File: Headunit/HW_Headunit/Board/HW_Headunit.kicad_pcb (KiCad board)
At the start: 2 copper layers, 27 x 30 mm, 4 parts, among them J1 AudioJack4_SwitchT1, J2 AudioJack4_SwitchT1, J3 2328702-8, U2 PY32F002AW15U

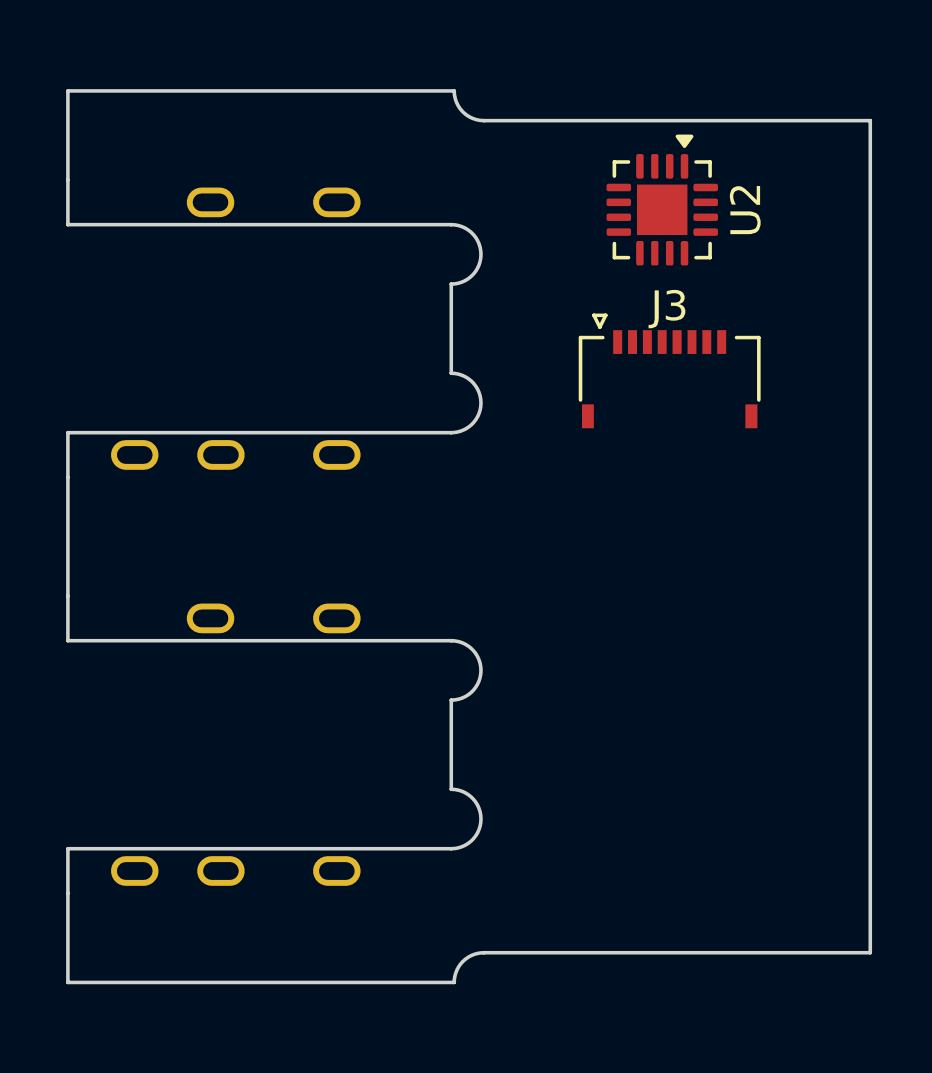
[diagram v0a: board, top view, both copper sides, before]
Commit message: PCB shape improved
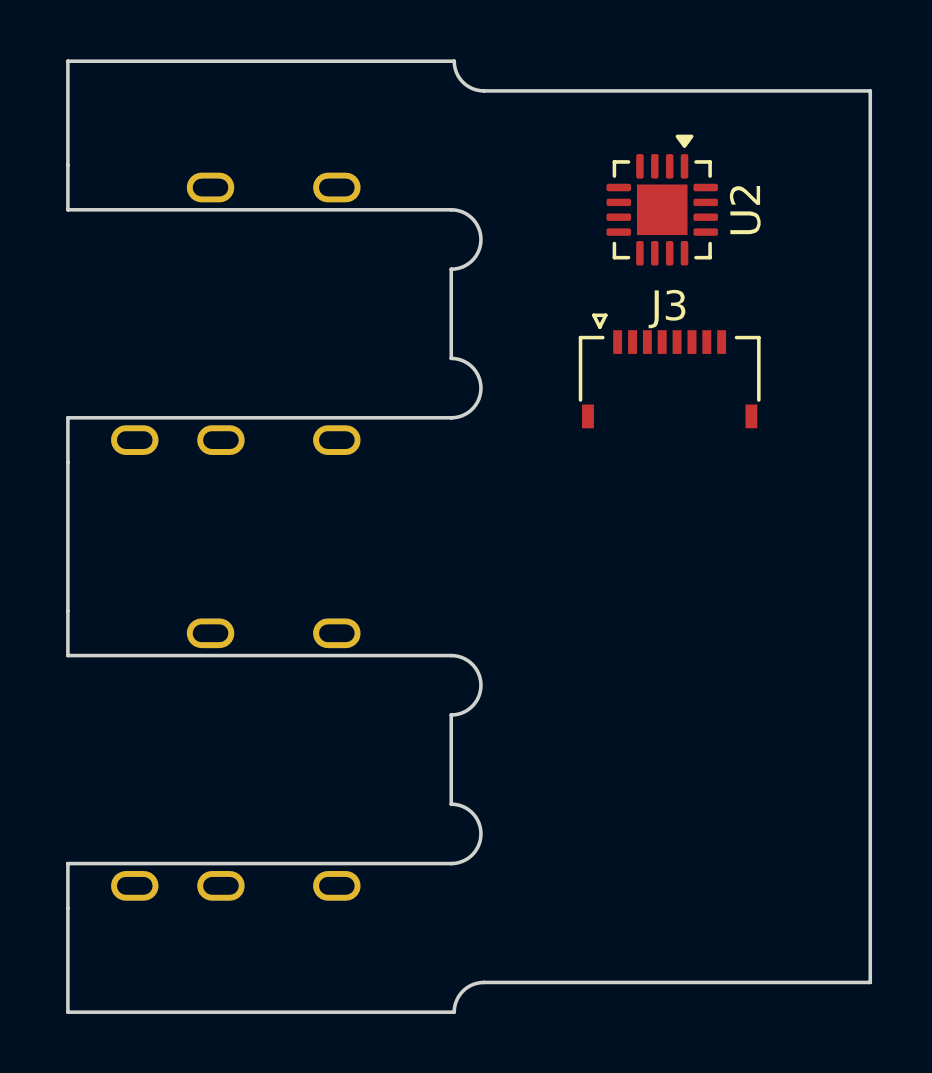
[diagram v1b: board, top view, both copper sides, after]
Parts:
- moved J1 0.50 mm to (0.00, 7.50)
- moved J2 0.50 mm to (0.00, -7.50)
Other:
- board size 27 x 30 mm -> 27 x 32 mm
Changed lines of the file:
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@@
 	(footprint "USER:XB-PJ-1837"
 		(layer "B.Cu")
-		(at 0 -7 -90)
+		(at 0 -7.5 -90)
 		(descr "TRS 3.5mm, horizontal, through-hole, https://www.cuidevices.com/product/resource/pdf/sj1-352xn.pdf")
 		(tags "TRS audio jack stereo horizontal")
@@
 	(footprint "USER:XB-PJ-1837"
 		(layer "B.Cu")
-		(at 0 7 -90)
+		(at 0 7.5 -90)
 		(descr "TRS 3.5mm, horizontal, through-hole, https://www.cuidevices.com/product/resource/pdf/sj1-352xn.pdf")
 		(tags "TRS audio jack stereo horizontal")
@@
 	)
 	(gr_line
-		(start 14 -14)
-		(end 27 -14)
+		(start 14.000001 -15)
+		(end 27.000001 -15)
 		(stroke
 			(width 0.12)
@@
 	)
 	(gr_line
-		(start 0 12)
-		(end 0 15)
+		(start 0 12.5)
+		(end 0 16)
 		(stroke
 			(width 0.12)
@@
 	)
 	(gr_arc
-		(start 13 15)
-		(mid 13.292893 14.292893)
-		(end 14 14)
+		(start 13 16)
+		(mid 13.292893 15.292893)
+		(end 14 15)
 		(stroke
 			(width 0.12)
@@
 	)
 	(gr_line
-		(start 0 -12)
-		(end 0 -15)
+		(start 0 -12.5)
+		(end 0 -16)
 		(stroke
 			(width 0.12)
@@
 	)
 	(gr_line
-		(start 27 14)
-		(end 27 -14)
+		(start 27 15)
+		(end 27.000001 -15)
 		(stroke
 			(width 0.12)
@@
 	)
 	(gr_line
-		(start 14 14)
-		(end 27 14)
+		(start 14 15)
+		(end 27 15)
 		(stroke
 			(width 0.12)
@@
 	)
 	(gr_line
-		(start 0 -15)
-		(end 13 -15)
+		(start 0 -16)
+		(end 13 -16)
 		(stroke
 			(width 0.12)
@@
 	)
 	(gr_arc
-		(start 13.999999 -14)
-		(mid 13.292893 -14.292894)
-		(end 12.999999 -15)
+		(start 14 -15)
+		(mid 13.292894 -15.292894)
+		(end 13 -16)
 		(stroke
 			(width 0.12)
@@
 	)
 	(gr_line
-		(start 0 15)
-		(end 13 15)
+		(start 0 16)
+		(end 13 16)
 		(stroke
 			(width 0.12)
@@
 	)
 	(gr_line
-		(start 0 2)
-		(end 0 -2)
-		(stroke
-			(width 0.12)
+		(start 0 2.5)
+		(end 0 -2.5)
+		(stroke
+			(width 0.12)

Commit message: Exported fabrication files
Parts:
- added C1: 1u, Capacitor_SMD:C_0603_1608Metric, F.Cu at (6.00, 14.2)
- added C2: 100n, Capacitor_SMD:C_0402_1005Metric, F.Cu at (3.00, 3.25)
- added C3: 100n, Capacitor_SMD:C_0402_1005Metric, F.Cu at (11.0, -1.00)
- added C4: 1u, Capacitor_SMD:C_0603_1608Metric, F.Cu at (16.0, -12.0)
- added C5: 100n, Capacitor_SMD:C_0402_1005Metric, F.Cu at (24.8, -8.50)
- added C6: 1u, Capacitor_SMD:C_0603_1608Metric, F.Cu at (18.8, 0.76)
- added C68: 100n, Capacitor_SMD:C_0402_1005Metric, F.Cu at (17.2, -14.2)
- added C7: 100n, Capacitor_SMD:C_0402_1005Metric, F.Cu at (2.75, -11.8)
- added C73: 1u, Capacitor_SMD:C_0603_1608Metric, F.Cu at (12.0, 14.2)
- added D1: SP0502BAHT, Package_TO_SOT_SMD:SOT-23, F.Cu at (3.25, 14.2)
- added F1: 0603L020YR, Fuse:Fuse_0603_1608Metric, F.Cu at (11.5, 11.8)
- added J4: HS096T01H13, USER:HS096T01H13, F.Cu at (20.2, 0.00)
- added J5: Conn_01x05, Connector_PinHeader_2.54mm:PinHeader_1x05_P2.54mm_Vertical, F.Cu at (11.6, -14.5)
- added Q2: DMC2400UV, Package_TO_SOT_SMD:SOT-563, F.Cu at (12.2, 1.75)
- added Q3: DMC2400UV, Package_TO_SOT_SMD:SOT-563, F.Cu at (3.00, 1.75)
- added R1: 62R, Resistor_SMD:R_0805_2012Metric, F.Cu at (4.00, -1.00)
- added R10: 10k, Resistor_SMD:R_0402_1005Metric, F.Cu at (6.50, 2.75)
- added R11: 10R, Resistor_SMD:R_0402_1005Metric, F.Cu at (14.8, -1.50)
- added R12: 10R, Resistor_SMD:R_0402_1005Metric, F.Cu at (14.8, -2.50)
- added R13: 10k, Resistor_SMD:R_0402_1005Metric, F.Cu at (14.8, -14.2)
- added R2: 62R, Resistor_SMD:R_0805_2012Metric, F.Cu at (2.00, -1.00)
- added R3: 10k, Resistor_SMD:R_0402_1005Metric, F.Cu at (14.8, 1.00)
- added R4: 10k, Resistor_SMD:R_0402_1005Metric, F.Cu at (4.75, 1.75)
- added R5: 10k, Resistor_SMD:R_0402_1005Metric, F.Cu at (11.0, -11.8)
- added R6: 10k, Resistor_SMD:R_0402_1005Metric, F.Cu at (6.75, -11.8)
- added R7: 10R, Resistor_SMD:R_0402_1005Metric, F.Cu at (14.8, 0.00)
- added R8: 10k, Resistor_SMD:R_0402_1005Metric, F.Cu at (24.8, -6.50)
- added R9: 10k, Resistor_SMD:R_0402_1005Metric, F.Cu at (7.75, 2.75)
- added REF**: OSHW-Logo_5.7x6mm_SilkScreen, Symbol:OSHW-Logo_5.7x6mm_SilkScreen, B.Cu at (23.5, 11.5)
- added TP1: G, TestPoint:TestPoint_Pad_D1.5mm, B.Cu at (17.5, -2.50)
- added TP2: 3, TestPoint:TestPoint_Pad_D1.5mm, B.Cu at (17.5, 12.5)
- added TP3: 5, TestPoint:TestPoint_Pad_D1.5mm, B.Cu at (17.5, 10.0)
- added TP4: H, TestPoint:TestPoint_Pad_D1.5mm, B.Cu at (7.50, 0.00)
- added TP5: L, TestPoint:TestPoint_Pad_D1.5mm, B.Cu at (2.50, 0.00)
- added TP6: T, TestPoint:TestPoint_Pad_D1.5mm, B.Cu at (17.5, -7.50)
- added TP7: R, TestPoint:TestPoint_Pad_D1.5mm, B.Cu at (17.5, -5.00)
- added TP8: A, TestPoint:TestPoint_Pad_D1.5mm, B.Cu at (17.5, -10.0)
- added TP9: B, TestPoint:TestPoint_Pad_D1.5mm, B.Cu at (10.0, 0.00)
- added U1: STM32L432KBUx, Package_DFN_QFN:QFN-32-1EP_5x5mm_P0.5mm_EP3.45x3.45mm, F.Cu at (21.5, -11.8)
- added U3: SIT1050TK, Package_DFN_QFN:DFN-8-1EP_3x3mm_P0.65mm_EP1.5x2.25mm, F.Cu at (8.00, -1.00)
- J1, J2: value AudioJack4_SwitchT1 -> XB-PJ-1837
- U2: value PY32F002AW15U -> XC6206P332MR-G; footprint Package_DFN_QFN:QFN-16-1EP_3x3mm_P0.5mm_EP1.7x1.7mm -> Package_TO_SOT_SMD:SOT-23-3
- moved U2 27.5 mm to (9.00, 14.2), turned to 0 degrees
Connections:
- net Net-(J1-Pad2) renamed /CAN_L
- net Net-(J1-Pad3) renamed /CAN_H
- J1 pad 4: +5V -> Net-(F1-Pad2)
- J1 pad 5: unconnected-(J1-Pad5) -> Net-(J1-Pad5)
- J2 pad 4: +5V -> Net-(F1-Pad2)
- J2 pad 5: unconnected-(J2-Pad5) -> Net-(J2-Pad5)
- J3 pad 1: unconnected-(J3-Pin_1-Pad1) -> Net-(J3-Pin_1)
- U2 pad 1: unconnected-(U2-PB1-Pad1) -> GND
- U2 pad 2: unconnected-(U2-PA12-Pad2) -> +3.3V
- U2 pad 3: unconnected-(U2-PA13-SWD-Pad3) -> +5V
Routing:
- net /CAN_L: track 0.00 -> 67.1 mm, vias 0 -> 2
- net /CAN_H: track 0.00 -> 67.0 mm, vias 0 -> 2
- net GND: track 0.00 -> 46.3 mm, vias 0 -> 21
- net /CAN_TERM: track 0.00 -> 43.5 mm
- net +5V: track 0.00 -> 32.5 mm, vias 0 -> 4
- net /LCD_PWM: track 0.00 -> 31.5 mm
- net /SWD: track 0.00 -> 28.0 mm, vias 0 -> 1
- net +3.3V: track 0.00 -> 26.8 mm, vias 0 -> 11
- net /DET_B: track 0.00 -> 24.2 mm, vias 0 -> 2
- net /LCD_CS: track 0.00 -> 23.4 mm, vias 0 -> 2
- net /CAN_TX: track 0.00 -> 22.7 mm, vias 0 -> 2
- net /SWC: track 0.00 -> 22.4 mm, vias 0 -> 1
- net /CAN_RX: track 0.00 -> 21.7 mm, vias 0 -> 2
- net /NRST: track 0.00 -> 20.3 mm
- net Net-(Q2A-D): track 0.00 -> 17.8 mm, vias 0 -> 2
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- added copper zone on In1.Cu, net +3.3V
- added copper zone on B.Cu, net GND
- added copper zone on F.Cu, net GND
- added copper zone on In1.Cu, net Net-(F1-Pad2)
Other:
- copper layers 2 -> 4
- board text added: "Project: ${TITLE} Rev.: ${REVISION} Date: ${CURRENT_DATE}"
